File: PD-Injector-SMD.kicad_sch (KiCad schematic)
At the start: 10 parts, among them P1 C-UTC09-00

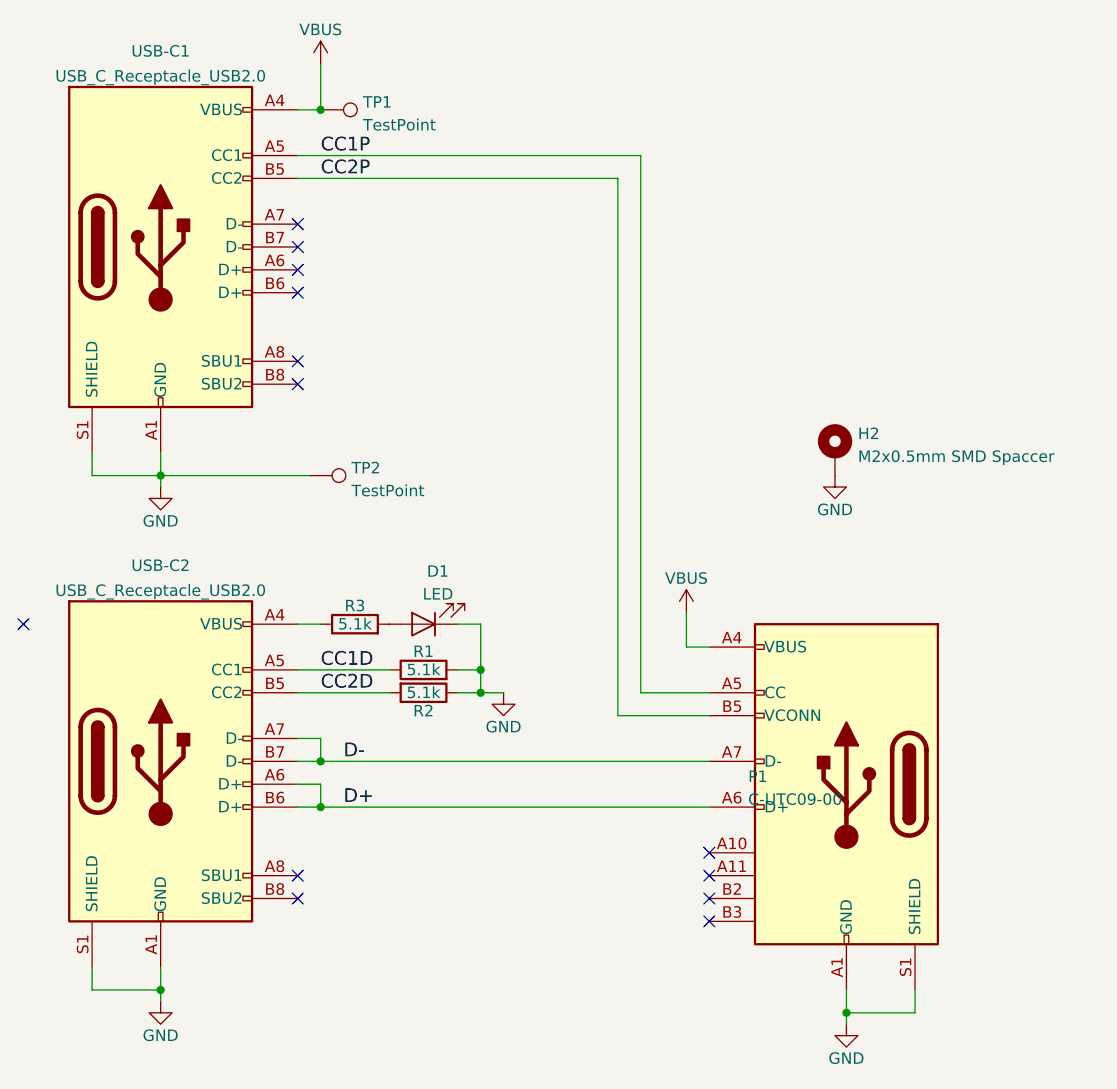
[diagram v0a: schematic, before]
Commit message: Swapped output to receptacle
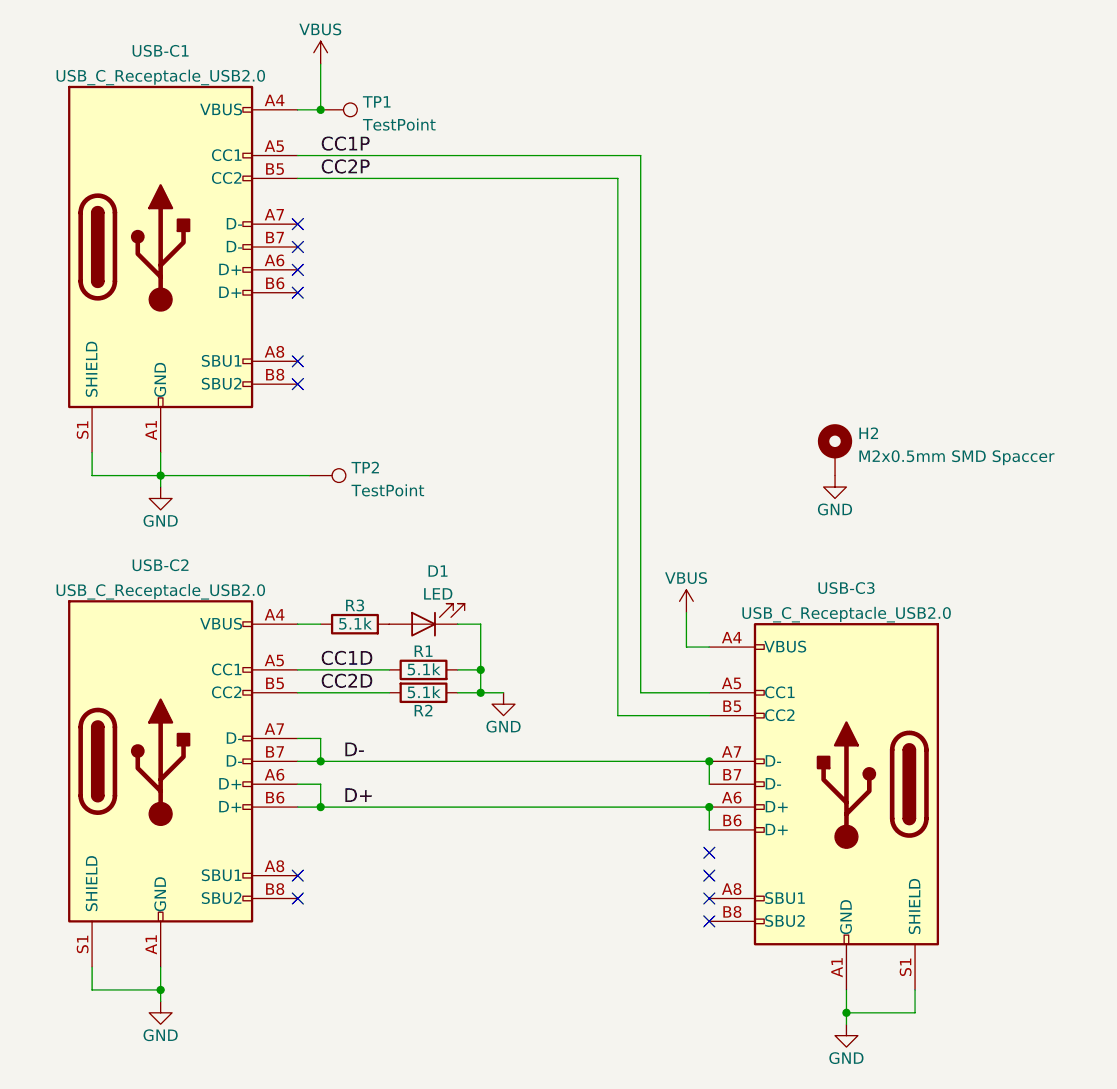
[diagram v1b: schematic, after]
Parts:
- removed P1: C-UTC09-00, Connector_USB_Extra:USB_C_Plug_UTC009-C12, symbol Connector:USB_C_Plug_USB2.0
- added USB-C3: USB_C_Receptacle_USB2.0, PD-Injector_SMD:USB_C_Receptacle_GT-USB-7010, symbol Connector:USB_C_Receptacle_USB2.0
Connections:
- net CC1P: now also USB-C3.A5 (CC1)
- net CC2P: now also USB-C3.B5 (CC2)
- net D+: now also USB-C3.A6 (D+), USB-C3.B6 (D+)
- net D-: now also USB-C3.A7 (D-), USB-C3.B7 (D-)
- net GND: now also USB-C3.A1 (GND), USB-C3.A12 (GND), USB-C3.B1 (GND), USB-C3.B12 (GND), USB-C3.S1 (SHIELD)
- net VBUS: now also USB-C3.A4 (VBUS), USB-C3.B9 (VBUS)
- new net: USB-C3.A9 (VBUS), USB-C3.B4 (VBUS)
- no-connect marks 13 -> 12
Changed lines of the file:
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@@
   (junction (at 99.06 97.79) (diameter 0) (color 0 0 0 0)
   )
+  (junction (at 160.02 134.62) (diameter 0) (color 0 0 0 0)
+  )
   (junction (at 99.06 154.94) (diameter 0) (color 0 0 0 0)
   )
@@
   )
   (junction (at 134.62 121.92) (diameter 0) (color 0 0 0 0)
+  )
+  (junction (at 160.02 129.54) (diameter 0) (color 0 0 0 0)
   )
   (junction (at 116.84 129.54) (diameter 0) (color 0 0 0 0)
@@
   (no_connect (at 160.02 147.32))
   (no_connect (at 114.3 142.24))
-  (no_connect (at 83.82 114.3))
   (wire (pts (xy 99.06 97.79) (xy 99.06 99.06))
     (stroke (width 0) (type default))
@@
     (stroke (width 0) (type default))
   )
+  (wire (pts (xy 160.02 134.62) (xy 160.02 137.16))
+    (stroke (width 0) (type default))
+  )
   (wire (pts (xy 116.84 134.62) (xy 116.84 132.08))
     (stroke (width 0) (type default))
   )
   (wire (pts (xy 157.48 116.84) (xy 160.02 116.84))
+    (stroke (width 0) (type default))
+  )
+  (wire (pts (xy 160.02 129.54) (xy 160.02 132.08))
     (stroke (width 0) (type default))
   )
@@
     )
   )
-  (symbol (lib_id "Connector:TestPoint") (at 116.84 57.15 270) (unit 1)
-    (in_bom yes) (on_board yes) (dnp no) (fields_autoplaced)
-    (property "Reference" "TP1" (at 121.539 56.3153 90)
-      (effects (font (size 1.27 1.27)) (justify left))
-    )
-    (property "Value" "TestPoint" (at 121.539 58.8522 90)
-      (effects (font (size 1.27 1.27)) (justify left))
-    )
-    (property "Footprint" "TestPoint:TestPoint_Pad_D2.0mm" (at 116.84 62.23 0)
-      (effects (font (size 1.27 1.27)) hide)
-    )
-    (property "Datasheet" "~" (at 116.84 62.23 0)
-      (effects (font (size 1.27 1.27)) hide)
-    )
-    (pin "1")
-    (instances
-      (project "PD-Injector-SMD"
-        (path "/9c9ff308-9f05-4495-8829-b9ddd550c875"
-          (reference "TP1") (unit 1)
-        )
-      )
-    )
-  )
-  (symbol (lib_id "Device:LED") (at 128.27 114.3 180) (unit 1)
-    (in_bom yes) (on_board yes) (dnp no) (fields_autoplaced)
-    (property "Reference" "D1" (at 129.8702 108.4412 0)
-      (effects (font (size 1.27 1.27)))
-    )
-    (property "Value" "LED" (at 129.8702 110.9781 0)
-      (effects (font (size 1.27 1.27)))
-    )
-    (property "Footprint" "LED_SMD:LED_0402_1005Metric" (at 128.27 114.3 0)
-      (effects (font (size 1.27 1.27)) hide)
-    )
-    (property "Datasheet" "~" (at 128.27 114.3 0)
-      (effects (font (size 1.27 1.27)) hide)
-    )
-    (pin "1")
-    (pin "2")
-    (instances
-      (project "PD-Injector-SMD"
-        (path "/9c9ff308-9f05-4495-8829-b9ddd550c875"
-          (reference "D1") (unit 1)
-        )
-      )
-    )
-  )
-  (symbol (lib_id "Connector:USB_C_Receptacle_USB2.0") (at 99.06 72.39 0) (unit 1)
-    (in_bom yes) (on_board yes) (dnp no) (fields_autoplaced)
-    (property "Reference" "USB-C1" (at 99.06 50.6435 0)
-      (effects (font (size 1.27 1.27)))
-    )
-    (property "Value" "USB_C_Receptacle_USB2.0" (at 99.06 53.4186 0)
-      (effects (font (size 1.27 1.27)))
-    )
-    (property "Footprint" "Connector_USB_Extra:USB_C_Receptacle_GT-USB-7010" (at 102.87 72.39 0)
-      (effects (font (size 1.27 1.27)) hide)
-    )
-    (property "Datasheet" "https://www.usb.org/sites/default/files/documents/usb_type-c.zip" (at 102.87 72.39 0)
+  (symbol (lib_name "USB_C_Receptacle_USB2.0_1") (lib_id "Connector:USB_C_Receptacle_USB2.0") (at 175.26 132.08 0) (mirror y) (unit 1)
+    (in_bom yes) (on_board yes) (dnp no)
+    (property "Reference" "USB-C3" (at 175.26 110.3335 0)
+      (effects (font (size 1.27 1.27)))
+    )
+    (property "Value" "USB_C_Receptacle_USB2.0" (at 175.26 113.1086 0)
+      (effects (font (size 1.27 1.27)))
+    )
+    (property "Footprint" "PD-Injector_SMD:USB_C_Receptacle_GT-USB-7010" (at 171.45 132.08 0)
+      (effects (font (size 1.27 1.27)) hide)
+    )
+    (property "Datasheet" "https://www.usb.org/sites/default/files/documents/usb_type-c.zip" (at 171.45 132.08 0)
       (effects (font (size 1.27 1.27)) hide)
     )
@@
       (project "PD-Injector-SMD"
         (path "/9c9ff308-9f05-4495-8829-b9ddd550c875"
-          (reference "USB-C1") (unit 1)
-        )
-      )
-    )
-  )
-  (symbol (lib_id "Connector:USB_C_Plug_USB2.0") (at 175.26 132.08 0) (mirror y) (unit 1)
+          (reference "USB-C3") (unit 1)
+        )
+      )
+    )
+  )
+  (symbol (lib_id "Connector:TestPoint") (at 116.84 57.15 270) (unit 1)
     (in_bom yes) (on_board yes) (dnp no) (fields_autoplaced)
-    (property "Reference" "P1" (at 164.338 131.2453 0)
-      (effects (font (size 1.27 1.27)) (justify right))
-    )
-    (property "Value" "C-UTC09-00" (at 164.338 133.7822 0)
-      (effects (font (size 1.27 1.27)) (justify right))
-    )
-    (property "Footprint" "Connector_USB_Extra:USB_C_Plug_UTC009-C12" (at 179.07 132.08 0)
-      (effects (font (size 1.27 1.27)) hide)
-    )
-    (property "Datasheet" "https://www.solder.party/docs/usb-c-pack/" (at 179.07 132.08 0)
+    (property "Reference" "TP1" (at 121.539 56.3153 90)
+      (effects (font (size 1.27 1.27)) (justify left))
+    )
+    (property "Value" "TestPoint" (at 121.539 58.8522 90)
+      (effects (font (size 1.27 1.27)) (justify left))
+    )
+    (property "Footprint" "TestPoint:TestPoint_Pad_D2.0mm" (at 116.84 62.23 0)
+      (effects (font (size 1.27 1.27)) hide)
+    )
+    (property "Datasheet" "~" (at 116.84 62.23 0)
+      (effects (font (size 1.27 1.27)) hide)
+    )
+    (pin "1")
+    (instances
+      (project "PD-Injector-SMD"
+        (path "/9c9ff308-9f05-4495-8829-b9ddd550c875"
+          (reference "TP1") (unit 1)
+        )
+      )
+    )
+  )
+  (symbol (lib_id "Device:LED") (at 128.27 114.3 180) (unit 1)
+    (in_bom yes) (on_board yes) (dnp no) (fields_autoplaced)
+    (property "Reference" "D1" (at 129.8702 108.4412 0)
+      (effects (font (size 1.27 1.27)))
+    )
+    (property "Value" "LED" (at 129.8702 110.9781 0)
+      (effects (font (size 1.27 1.27)))
+    )
+    (property "Footprint" "LED_SMD:LED_0402_1005Metric" (at 128.27 114.3 0)
+      (effects (font (size 1.27 1.27)) hide)
+    )
+    (property "Datasheet" "~" (at 128.27 114.3 0)
+      (effects (font (size 1.27 1.27)) hide)
+    )
+    (pin "1")
+    (pin "2")
+    (instances
+      (project "PD-Injector-SMD"
+        (path "/9c9ff308-9f05-4495-8829-b9ddd550c875"
+          (reference "D1") (unit 1)
+        )
+      )
+    )
+  )
+  (symbol (lib_id "Connector:USB_C_Receptacle_USB2.0") (at 99.06 72.39 0) (unit 1)
+    (in_bom yes) (on_board yes) (dnp no) (fields_autoplaced)
+    (property "Reference" "USB-C1" (at 99.06 50.6435 0)
+      (effects (font (size 1.27 1.27)))
+    )
+    (property "Value" "USB_C_Receptacle_USB2.0" (at 99.06 53.4186 0)
+      (effects (font (size 1.27 1.27)))
+    )
+    (property "Footprint" "Connector_USB_Extra:USB_C_Receptacle_GT-USB-7010" (at 102.87 72.39 0)
+      (effects (font (size 1.27 1.27)) hide)
+    )
+    (property "Datasheet" "https://www.usb.org/sites/default/files/documents/usb_type-c.zip" (at 102.87 72.39 0)
       (effects (font (size 1.27 1.27)) hide)
     )
     (pin "A1")
-    (pin "A10")
-    (pin "A11")
+    (pin "A12")
     (pin "A4")
     (pin "A5")
     (pin "A6")
     (pin "A7")
+    (pin "A8")
+    (pin "A9")
+    (pin "B1")
     (pin "B12")
-    (pin "B2")
-    (pin "B3")
+    (pin "B4")
     (pin "B5")
+    (pin "B6")
+    (pin "B7")
+    (pin "B8")
     (pin "B9")
     (pin "S1")
@@
       (project "PD-Injector-SMD"
         (path "/9c9ff308-9f05-4495-8829-b9ddd550c875"
-          (reference "P1") (unit 1)
-        )
-      )
+          (reference "USB-C1") (unit 1)
+        )
+      )

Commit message: Update readme, minor mucking about
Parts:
- USB-C1, USB-C2: value USB_C_Receptacle_USB2.0 -> USB-C USB2.0 PD; footprint Connector_USB_Extra:USB_C_Receptacle_GT-USB-7010 -> PD-Injector_SMD:USB_C_Receptacle_GT-USB-7010; symbol Connector:USB_C_Receptacle_USB2.0 -> PD-Injector-SMD:USB_C_Receptacle_USB2.0
- USB-C3: value USB_C_Receptacle_USB2.0 -> USB-C USB2.0 PD; symbol Connector:USB_C_Receptacle_USB2.0 -> PD-Injector-SMD:USB_C_Receptacle_USB2.0
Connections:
- net VBUS: now also USB-C3.A9 (VBUS), USB-C3.B4 (VBUS)
- net at R3.1, USB-C2.A4 (VBUS), USB-C2.B9 (VBUS): now also USB-C2.A9 (VBUS), USB-C2.B4 (VBUS)
- no-connect marks 12 -> 4
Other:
- moved on the sheet: TP2
